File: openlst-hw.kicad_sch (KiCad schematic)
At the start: 101 parts, among them J10 EXT 5V, J11 EXT VRF, J12 EXT VBAT, J2 EXT 3V3, J3 UART0, J4 UART1, J5 Switch Select, J6 Control Outputs, J7 CC Prog/Debug, J8 Conn_Coaxial, J9 ANT, U2 CC1110, U3 0433BM15A0001, U4 MIC803, U5 PE4250MLI, U6 PE4250MLI, U7 SF2446E, U8 RFFM6406, X1 TG2520SMN 27MHz

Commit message: change footprint to 80x80mm to fit cubesat 1U more comfortabley
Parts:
- H1, H2, H3, H4: footprint MountingHole:MountingHole_3.2mm_M3_Pad_Via -> Project:MountingHole_4.3mm_M4_Pad_Via_Custom
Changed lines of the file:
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@@
 			)
 		)
-		(property "Footprint" "MountingHole:MountingHole_3.2mm_M3_Pad_Via"
+		(property "Footprint" "Project:MountingHole_4.3mm_M4_Pad_Via_Custom"
 			(at 275.59 228.6 0)
 			(effects
@@
 			)
 		)
-		(property "Footprint" "MountingHole:MountingHole_3.2mm_M3_Pad_Via"
+		(property "Footprint" "Project:MountingHole_4.3mm_M4_Pad_Via_Custom"
 			(at 275.59 233.68 0)
 			(effects
@@
 			)
 		)
-		(property "Footprint" "MountingHole:MountingHole_3.2mm_M3_Pad_Via"
+		(property "Footprint" "Project:MountingHole_4.3mm_M4_Pad_Via_Custom"
 			(at 275.59 238.76 0)
 			(effects
@@
 			)
 		)
-		(property "Footprint" "MountingHole:MountingHole_3.2mm_M3_Pad_Via"
+		(property "Footprint" "Project:MountingHole_4.3mm_M4_Pad_Via_Custom"
 			(at 275.59 243.84 0)
 			(effects

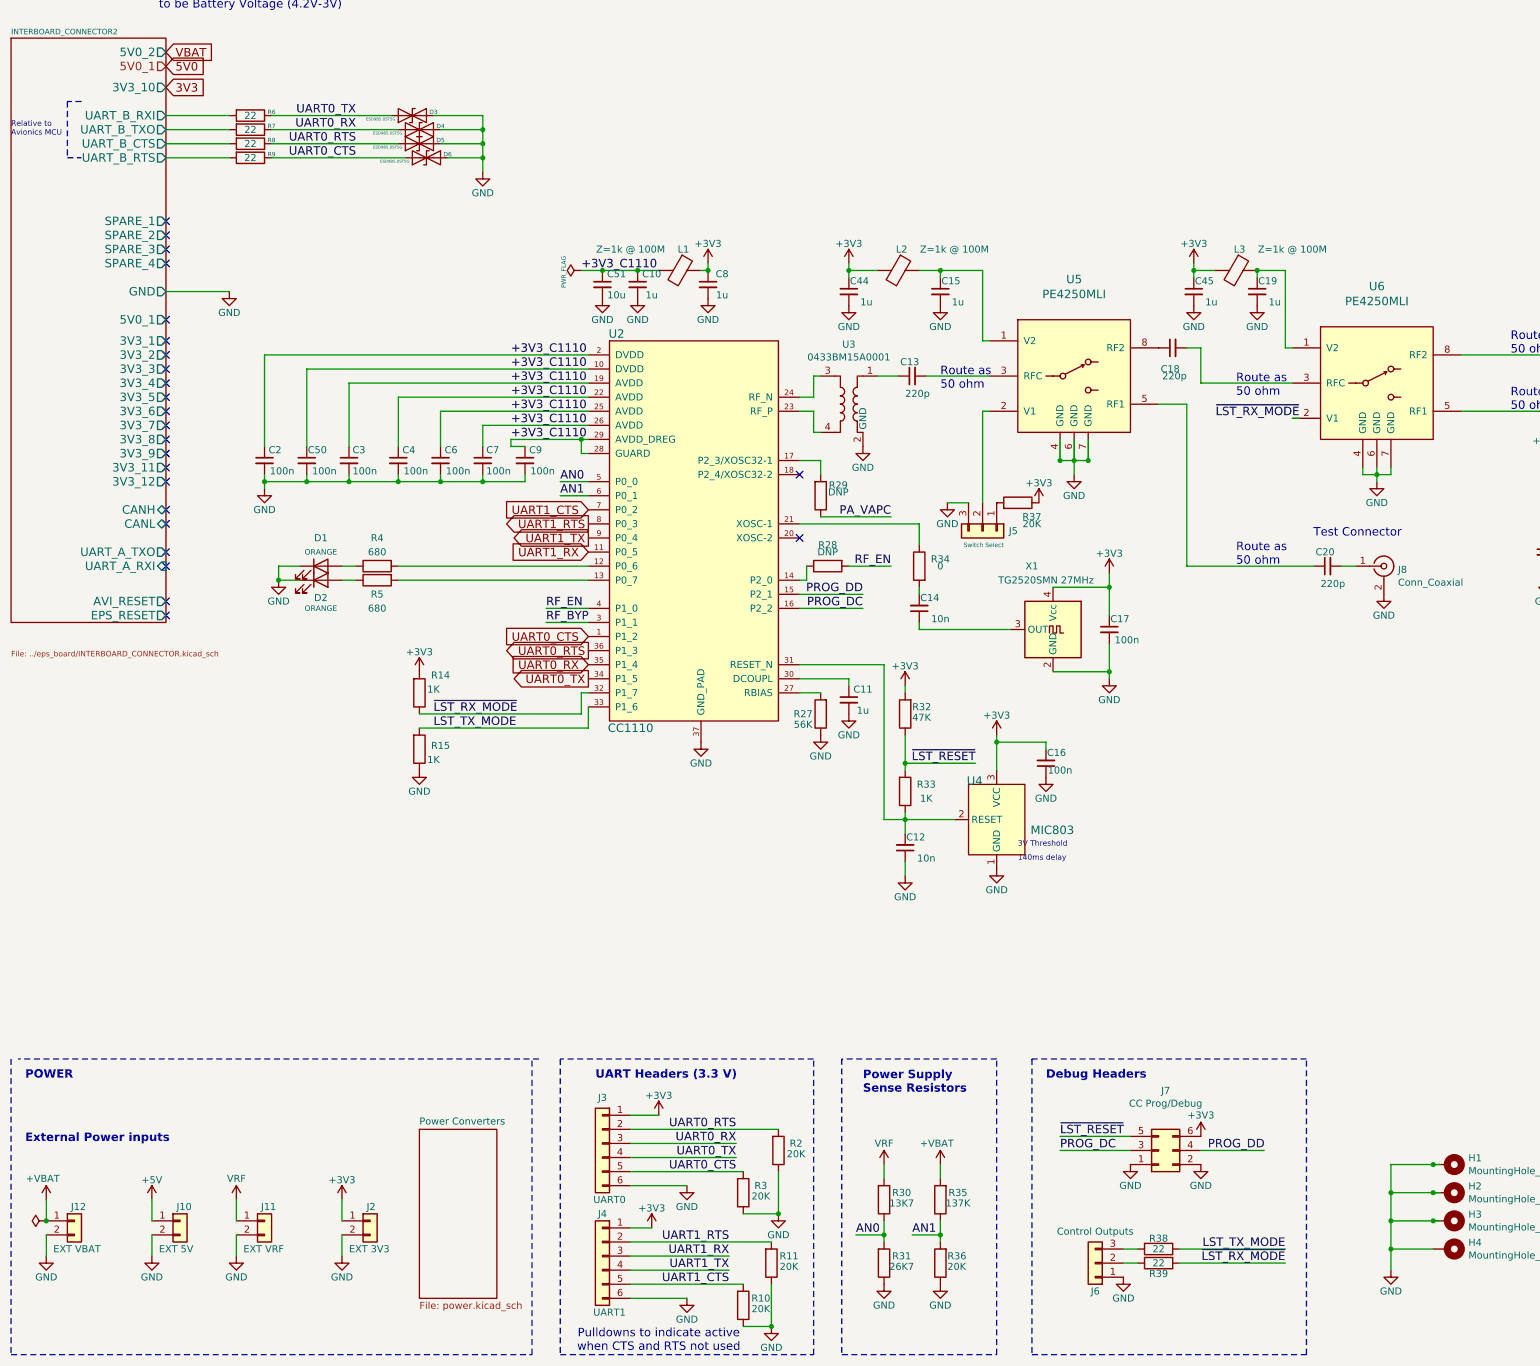
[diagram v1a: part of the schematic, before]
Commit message: add CAN bridge, change bus connector from 2x20 to 2x24 to allow second can bus and battery
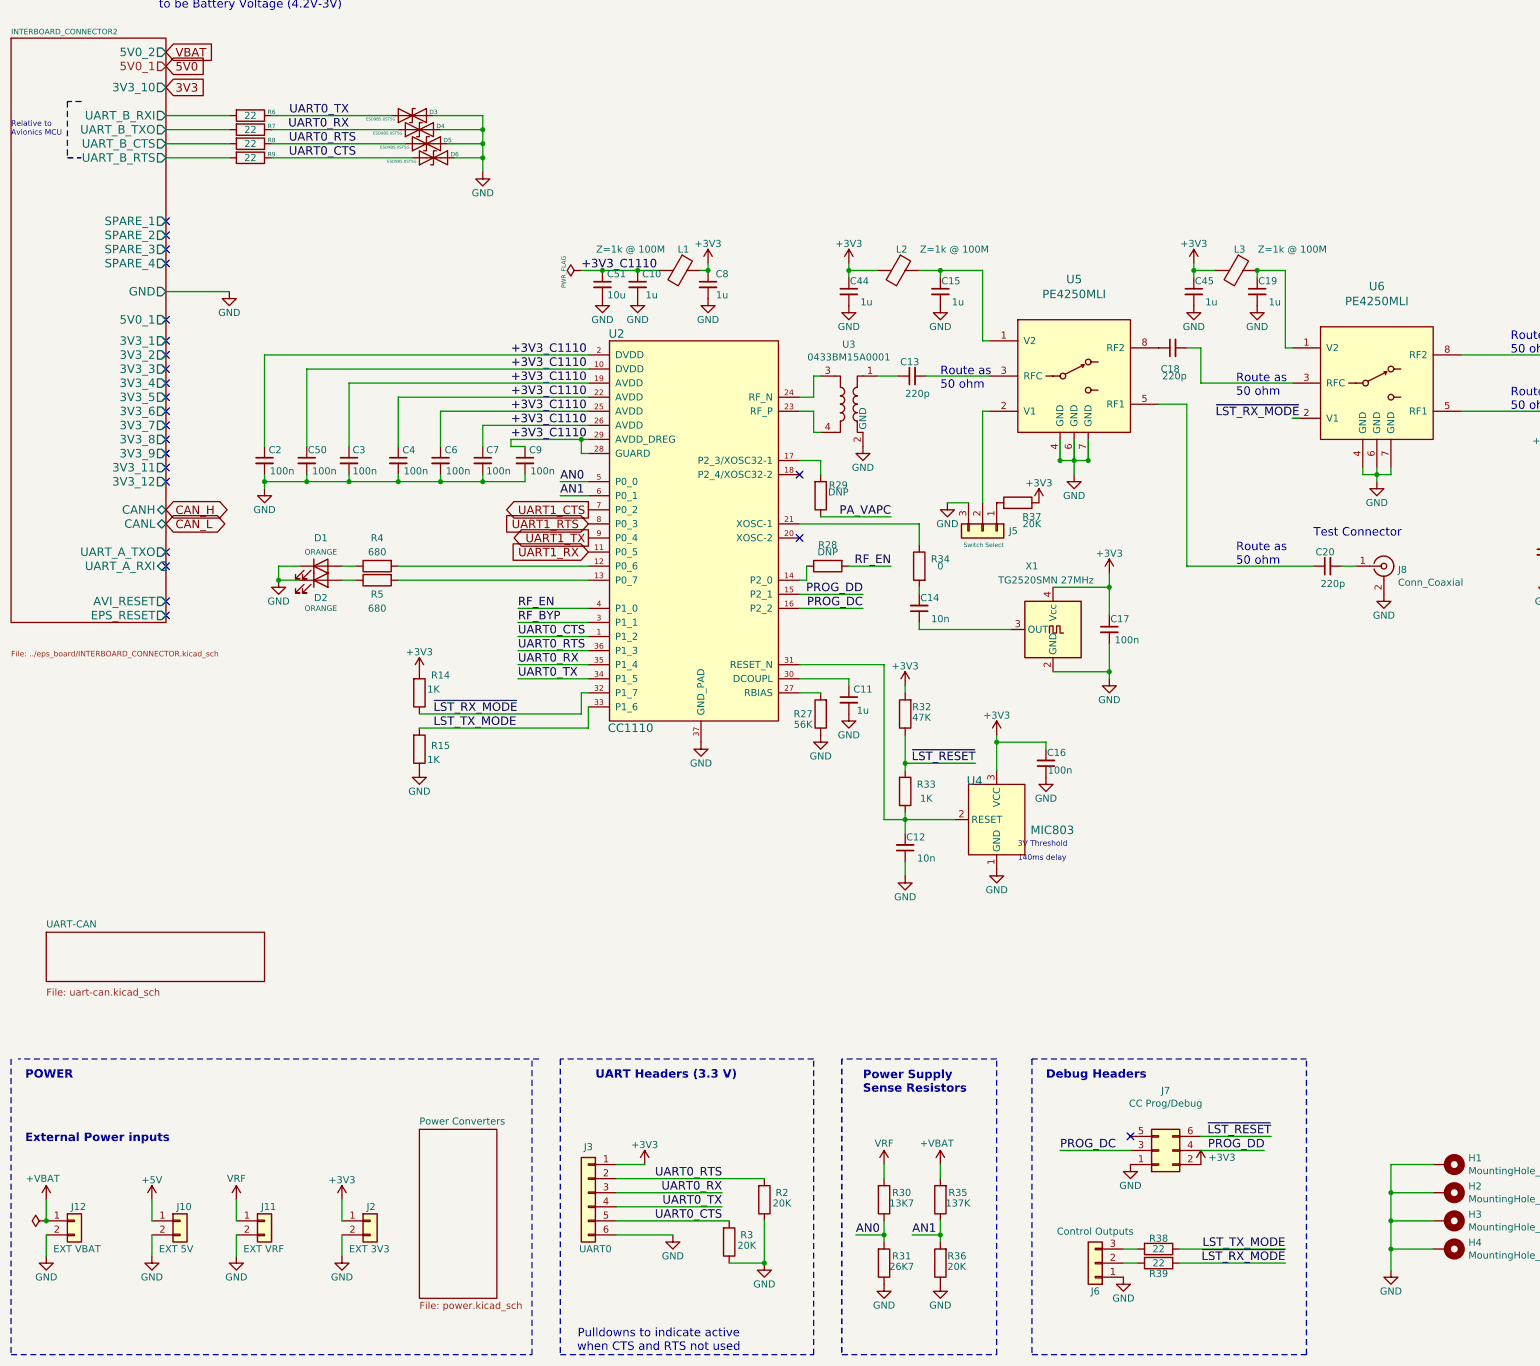
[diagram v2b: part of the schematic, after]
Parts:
- removed J4: UART1, Connector_PinHeader_2.54mm:PinHeader_1x06_P2.54mm_Vertical, symbol Connector_Generic:Conn_01x06
- removed R10, R11: 20K, Resistor_SMD:R_0603_1608Metric_Pad0.98x0.95mm_HandSolder, symbol Device:R
- J7: footprint Connector_PinHeader_2.54mm:PinHeader_2x03_P2.54mm_Vertical_SMD -> Connector_PinHeader_2.54mm:PinHeader_2x03_P2.54mm_Vertical
- J8, J9: footprint Connector_Coaxial:SMA_Amphenol_901-144_Vertical -> Project:LINX_CONSMA001-G
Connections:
- net +3V3: now also J7.2 (Pin_2); no longer J7.6 (Pin_6)
- net GND: no longer J7.2 (Pin_2)
- net ~{LST_RESET}: now also J7.6 (Pin_6); no longer J7.5 (Pin_5)
- no-connect marks 27 -> 26
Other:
- added sheet UART-CAN (uart-can.kicad_sch)
- moved on the sheet: D5, D6, J3, R2, R3

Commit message: cleanup, logical arrangement of connectors, short paths where possible and step files for all components
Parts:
- removed J10: EXT 5V, Connector_PinHeader_2.54mm:PinHeader_1x02_P2.54mm_Vertical, symbol Connector_Generic:Conn_01x02
- removed J11: EXT VRF, Connector_PinHeader_2.54mm:PinHeader_1x02_P2.54mm_Vertical, symbol Connector_Generic:Conn_01x02
- removed J12: EXT VBAT, Connector_PinHeader_2.54mm:PinHeader_1x02_P2.54mm_Vertical, symbol Connector_Generic:Conn_01x02
- removed J2: EXT 3V3, Connector_PinHeader_2.54mm:PinHeader_1x02_P2.54mm_Vertical, symbol Connector_Generic:Conn_01x02
- removed J3: UART0, Connector_PinHeader_2.54mm:PinHeader_1x06_P2.54mm_Vertical, symbol Connector_Generic:Conn_01x06
- added J5: UART0, Connector_PinHeader_2.54mm:PinHeader_1x06_P2.54mm_Vertical, symbol Connector_Generic:Conn_01x06
- added J6: EXT VBAT, Connector_PinHeader_2.54mm:PinHeader_1x02_P2.54mm_Vertical, symbol Connector_Generic:Conn_01x02
- added J7: EXT 5V, Connector_PinHeader_2.54mm:PinHeader_1x02_P2.54mm_Vertical, symbol Connector_Generic:Conn_01x02
- added J8: EXT VRF, Connector_PinHeader_2.54mm:PinHeader_1x02_P2.54mm_Vertical, symbol Connector_Generic:Conn_01x02
- added J9: EXT 3V3, Connector_PinHeader_2.54mm:PinHeader_1x02_P2.54mm_Vertical, symbol Connector_Generic:Conn_01x02
- renumbered C46 to C1, C51 to C10, C10 to C11, C8 to C12, C27 to C13, C29 to C14, C32 to C15, C44 to C16, C15 to C17, C45 to C18, C24 to C2, C18 to C20, C22 to C21, C13 to C22, C2 to C24, C50 to C25, C3 to C26, C4 to C27, C6 to C28, C7 to C29, C47 to C3, C9 to C30, C30 to C31, C21 to C32, C52 to C33, C20 to C34, C14 to C35, C17 to C36, C11 to C37, C16 to C38, C12 to C39, C48 to C4, C49 to C5, C26 to C6, C28 to C7, C31 to C8, C25 to C9, D3 to D1, D4 to D2, D5 to D3, D6 to D4, D1 to D5, D2 to D6, J9 to J1, J6 to J10, J5 to J2, J8 to J3, J7 to J4, L4 to L1, L1 to L2, L2 to L3, L3 to L4, R46 to R1, R4 to R10, R28 to R11, R34 to R12, R45 to R13, R5 to R14, R14 to R15, R27 to R16, R32 to R17, R15 to R18, R33 to R19, R47 to R2, R2 to R20, R30 to R21, R35 to R22, R3 to R23, R38 to R24, R31 to R25, R36 to R26, R39 to R27, R6 to R3, R7 to R4, R8 to R5, R9 to R6, R29 to R7, R44 to R8, R37 to R9, U7 to U1, U5 to U2, U6 to U3, U3 to U4, U8 to U5, U2 to U6, U4 to U7
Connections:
- net +3V3: now also J5.6 (Pin_6), J9.2 (Pin_2)
- net +5V: now also J7.2 (Pin_2)
- net +VBAT: now also J6.2 (Pin_2)
- net GND: now also J2.1 (Pin_1), J5.1 (Pin_1), J6.1 (Pin_1), J7.1 (Pin_1), J8.1 (Pin_1), J9.1 (Pin_1); no longer J2.3 (Pin_3)
- net UART0_CTS: now also J5.2 (Pin_2)
- net UART0_RTS: now also J5.5 (Pin_5)
- net UART0_RX: now also J5.4 (Pin_4)
- net UART0_TX: now also J5.3 (Pin_3)
- net at R9.2: now also J2.3 (Pin_3); no longer J2.1 (Pin_1)
- net VRF renamed +VRF
- net +VRF: now also J8.2 (Pin_2)
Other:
- sheet INTERBOARD_CONNECTOR2 ports: added BATT, CAN1H, CAN1L; removed 5V0_2, CANH, CANL
- note added: "+VRF = 4.2V to 2.5V"
- note removed: "5V0_2 is being modified to be Battery Voltage (4.2V-3V)"
- note removed: "VRF = 4.2V to 2.5V"
- moved on the sheet: J2

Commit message: break out RF part to separate schema, update BOM
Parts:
- removed C1, C16, C17, C18, C19, C2: 1u, Capacitor_SMD:C_0603_1608Metric_Pad1.08x0.95mm_HandSolder, symbol Device:C_Small
- removed C13, C3, C32, C6, C9: 100n, Capacitor_SMD:C_0402_1005Metric_Pad0.74x0.62mm_HandSolder, symbol Device:C_Small
- removed C14, C33, C4, C7: 10u, Capacitor_SMD:C_0603_1608Metric_Pad1.08x0.95mm_HandSolder, symbol Device:C_Small
- removed C15, C5, C8: 47u, Capacitor_SMD:C_0603_1608Metric_Pad1.08x0.95mm_HandSolder, symbol Device:C_Small
- removed C20, C21, C22, C23, C31, C34: 220p, Capacitor_SMD:C_0603_1608Metric_Pad1.08x0.95mm_HandSolder, symbol Device:C_Small
- removed J1: ANT, Project:LINX_CONSMA001-G, symbol Connector:Conn_Coaxial
- removed J2: Switch Select, Connector_PinHeader_2.54mm:PinHeader_1x03_P2.54mm_Vertical, symbol Connector_Generic:Conn_01x03
- removed J3: Conn_Coaxial, Project:LINX_CONSMA001-G, symbol Connector:Conn_Coaxial
- removed J6: EXT VBAT, Connector_PinHeader_2.54mm:PinHeader_1x02_P2.54mm_Vertical, symbol Connector_Generic:Conn_01x02
- removed J7: EXT 5V, Connector_PinHeader_2.54mm:PinHeader_1x02_P2.54mm_Vertical, symbol Connector_Generic:Conn_01x02
- removed J8: EXT VRF, Connector_PinHeader_2.54mm:PinHeader_1x02_P2.54mm_Vertical, symbol Connector_Generic:Conn_01x02
- removed J9: EXT 3V3, Connector_PinHeader_2.54mm:PinHeader_1x02_P2.54mm_Vertical, symbol Connector_Generic:Conn_01x02
- removed L1, L3, L4: Z=1k @ 100M, Inductor_SMD:L_0603_1608Metric_Pad1.05x0.95mm_HandSolder, symbol Device:FerriteBead
- removed R1: 3.09K, Resistor_SMD:R_0603_1608Metric_Pad0.98x0.95mm_HandSolder, symbol Device:R
- removed R13, R8: 1K, Resistor_SMD:R_0603_1608Metric_Pad0.98x0.95mm_HandSolder, symbol Device:R
- removed R2: 6.65K, Resistor_SMD:R_0603_1608Metric_Pad0.98x0.95mm_HandSolder, symbol Device:R
- removed R9: 20K, Resistor_SMD:R_0603_1608Metric_Pad0.98x0.95mm_HandSolder, symbol Device:R
- removed U1: SF2446E, Project:SF2446E, symbol Project:SF2446
- removed U2, U3: PE4250MLI, Package_SO:MSOP-8_3x3mm_P0.65mm, symbol Project:PE4259
- removed U4: 0433BM15A0001, RF_Converter:Balun_Johanson_0896BM15A0001, symbol Transformer:0433BM15A0001
- removed U5: RFFM6406, Project:RFFM6406, symbol Project:RFFM6403
- C1: renamed from C10; Manufactorer (none) -> Murata; Part Number (none) -> GRM21BR61E106KA73L; Tolerance (none) -> 10%; Voltage 10V -> 25
- C10: renamed from C30; Manufactorer (none) -> Murata; Part Number (none) -> GRM155R61E104KA87D; Tolerance (none) -> 10%; Voltage 25V -> 25
- C11: renamed from C35; Manufactorer (none) -> Murata; Part Number (none) -> GRT1885C1E103JA02J; Tolerance (none) -> 5%; Voltage 50V -> 25
- C12: renamed from C36; Manufactorer (none) -> Murata; Part Number (none) -> GRM155R61E104KA87D; Tolerance (none) -> 10%; Voltage 25V -> 25
- C13: renamed from C38; Manufactorer (none) -> Murata; Part Number (none) -> GRM155R61E104KA87D; Tolerance (none) -> 10%; Voltage 25V -> 25
- C14: renamed from C39; Manufactorer (none) -> Murata; Part Number (none) -> GRT1885C1E103JA02J; Tolerance (none) -> 5%; Voltage 50V -> 25
- C15: renamed from C37; Manufactorer (none) -> YAGEO; Part Number (none) -> CC0603KRX5R8BB105; Tolerance (none) -> 10%; Voltage 10V -> 25
- C2: renamed from C11; Manufactorer (none) -> YAGEO; Part Number (none) -> CC0603KRX5R8BB105; Tolerance (none) -> 10%; Voltage 10V -> 25
- C3: renamed from C12; Manufactorer (none) -> YAGEO; Part Number (none) -> CC0603KRX5R8BB105; Tolerance (none) -> 10%; Voltage 10V -> 25
- C4: renamed from C24; Manufactorer (none) -> Murata; Part Number (none) -> GRM155R61E104KA87D; Tolerance (none) -> 10%; Voltage 25V -> 25
- C5: renamed from C25; Manufactorer (none) -> Murata; Part Number (none) -> GRM155R61E104KA87D; Tolerance (none) -> 10%; Voltage 25V -> 25
- C6: renamed from C26; Manufactorer (none) -> Murata; Part Number (none) -> GRM155R61E104KA87D; Tolerance (none) -> 10%; Voltage 200V -> 25
- C7: renamed from C27; Manufactorer (none) -> Murata; Part Number (none) -> GRM155R61E104KA87D; Tolerance (none) -> 10%; Voltage 25V -> 25
- C8: renamed from C28; Manufactorer (none) -> Murata; Part Number (none) -> GRM155R61E104KA87D; Tolerance (none) -> 10%; Voltage 25V -> 25
- C9: renamed from C29; Manufactorer (none) -> Murata; Part Number (none) -> GRM155R61E104KA87D; Tolerance (none) -> 10%; Voltage 200V -> 25
- D1, D2, D3, D4: Manufactorer (none) -> onsemi; Part Number (none) -> ESD9B5.0ST5G
- D5, D6: Manufactorer (none) -> Lite-On; Part Number (none) -> LTST-C191KFKT; Voltage (none) -> 2.1
- FB1: renamed from L2; Amps (none) -> 1; Manufactorer (none) -> Murata; Part Number (none) -> BLM18KG102SN1D
- R1: renamed from R3; Manufactorer (none) -> YAGEO; Part Number (none) -> RC0603FR-0722RL; Tolerance (none) -> 1%
- R10: renamed from R11; value DNP -> 0; Manufactorer (none) -> YAGEO; Part Number (none) -> RC0603FR-070RL; now not fitted
- R11: renamed from R19; Manufactorer (none) -> YAGEO; Part Number (none) -> RC0603FR-071KL; Tolerance (none) -> 1%
- R12: renamed from R15; Manufactorer (none) -> YAGEO; Part Number (none) -> RC0603FR-071KL; Tolerance (none) -> 1%
- R13: renamed from R16; Manufactorer (none) -> YAGEO; Part Number (none) -> RC0603FR-0756KL; Tolerance (none) -> 1%
- R14: renamed from R18; Manufactorer (none) -> YAGEO; Part Number (none) -> RC0603FR-071KL; Tolerance (none) -> 1%
- R15: renamed from R20; Manufactorer (none) -> YAGEO; Part Number (none) -> RT0603BRD0720KL; Tolerance (none) -> 0.1%
- R16: renamed from R21; Manufactorer (none) -> YAGEO; Part Number (none) -> RT0603BRD0713K7L; Tolerance (none) -> 0.1%
- R17: renamed from R22; Manufactorer (none) -> YAGEO; Part Number (none) -> RT0603BRD07137KL; Tolerance (none) -> 0.1%
- R18: renamed from R23; Manufactorer (none) -> YAGEO; Part Number (none) -> RT0603BRD0720KL; Tolerance (none) -> 0.1%
- R19: renamed from R24; Manufactorer (none) -> YAGEO; Part Number (none) -> RC0603FR-0722RL; Tolerance (none) -> 1%
- R2: renamed from R4; Manufactorer (none) -> YAGEO; Part Number (none) -> RC0603FR-0722RL; Tolerance (none) -> 1%
- R20: renamed from R25; Manufactorer (none) -> YAGEO; Part Number (none) -> RT0603BRD0726K7L; Tolerance (none) -> 0.1%
- R21: renamed from R26; Manufactorer (none) -> YAGEO; Part Number (none) -> RT0603BRD0720KL; Tolerance (none) -> 0.1%
- R22: renamed from R27; Manufactorer (none) -> YAGEO; Part Number (none) -> RC0603FR-0722RL; Tolerance (none) -> 1%
- R3: renamed from R5; Manufactorer (none) -> YAGEO; Part Number (none) -> RC0603FR-0722RL; Tolerance (none) -> 1%
- R4: renamed from R6; Manufactorer (none) -> YAGEO; Part Number (none) -> RC0603FR-0722RL; Tolerance (none) -> 1%
- R5: renamed from R7; value DNP -> 0; Manufactorer (none) -> YAGEO; Part Number (none) -> RC0603FR-070RL; now not fitted
- R6: renamed from R12; Manufactorer (none) -> YAGEO; Part Number (none) -> RC0603FR-070RL
- R7: renamed from R10; Manufactorer (none) -> YAGEO; Part Number (none) -> RC0603FR-07680RL; Tolerance (none) -> 1%
- R8: renamed from R17; Manufactorer (none) -> YAGEO; Part Number (none) -> RC0603FR-0747KL; Tolerance (none) -> 1%
- R9: renamed from R14; Manufactorer (none) -> YAGEO; Part Number (none) -> RC0603FR-07680RL; Tolerance (none) -> 1%
- renumbered J4 to J1, J5 to J2, J10 to J7, U6 to U1, U7 to U2
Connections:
- net PA_VAPC: now also R5.2; no longer R5.1
- net at U1.17 (P2_3/XOSC32-1): now also R5.1; no longer R5.2
- net RF_P: now reaches U1.23 (RF_P)
- net RF_N: now reaches U1.24 (RF_N)
- net ~{LST_RESET} renamed LST_RESET
- net ~{LST_RX_MODE} renamed LST_RX_MODE
- no-connect marks 26 -> 23
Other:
- added sheet RF (rf.kicad_sch)
- note removed: "+VRF = 4.2V to 2.5V"
- note removed: "External Power inputs"
- note removed: "ICC worst case = 1.2A"
- note removed: "Nominal Vapc = 2.25V @ 60uA"
- note removed: "POWER"
- note removed: "Route as 50 ohm"
- note removed: "Test Connector"
- moved on the sheet: C1, C10, C11, C12, C13, C14, C15, C2, C3, C4, C5, C6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
